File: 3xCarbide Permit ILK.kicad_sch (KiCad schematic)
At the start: 48 parts, among them J1 UT00104PH, J2 UT00104PH, J3 UT00104PH, J4 UT00104PH, J5 UT00104PH, J6 UT00104PH, SW1 2PB11, SW2 2PB11, SW3 2PB11, SW4 2PB11, SW5 2PB11, SW6 2PB11

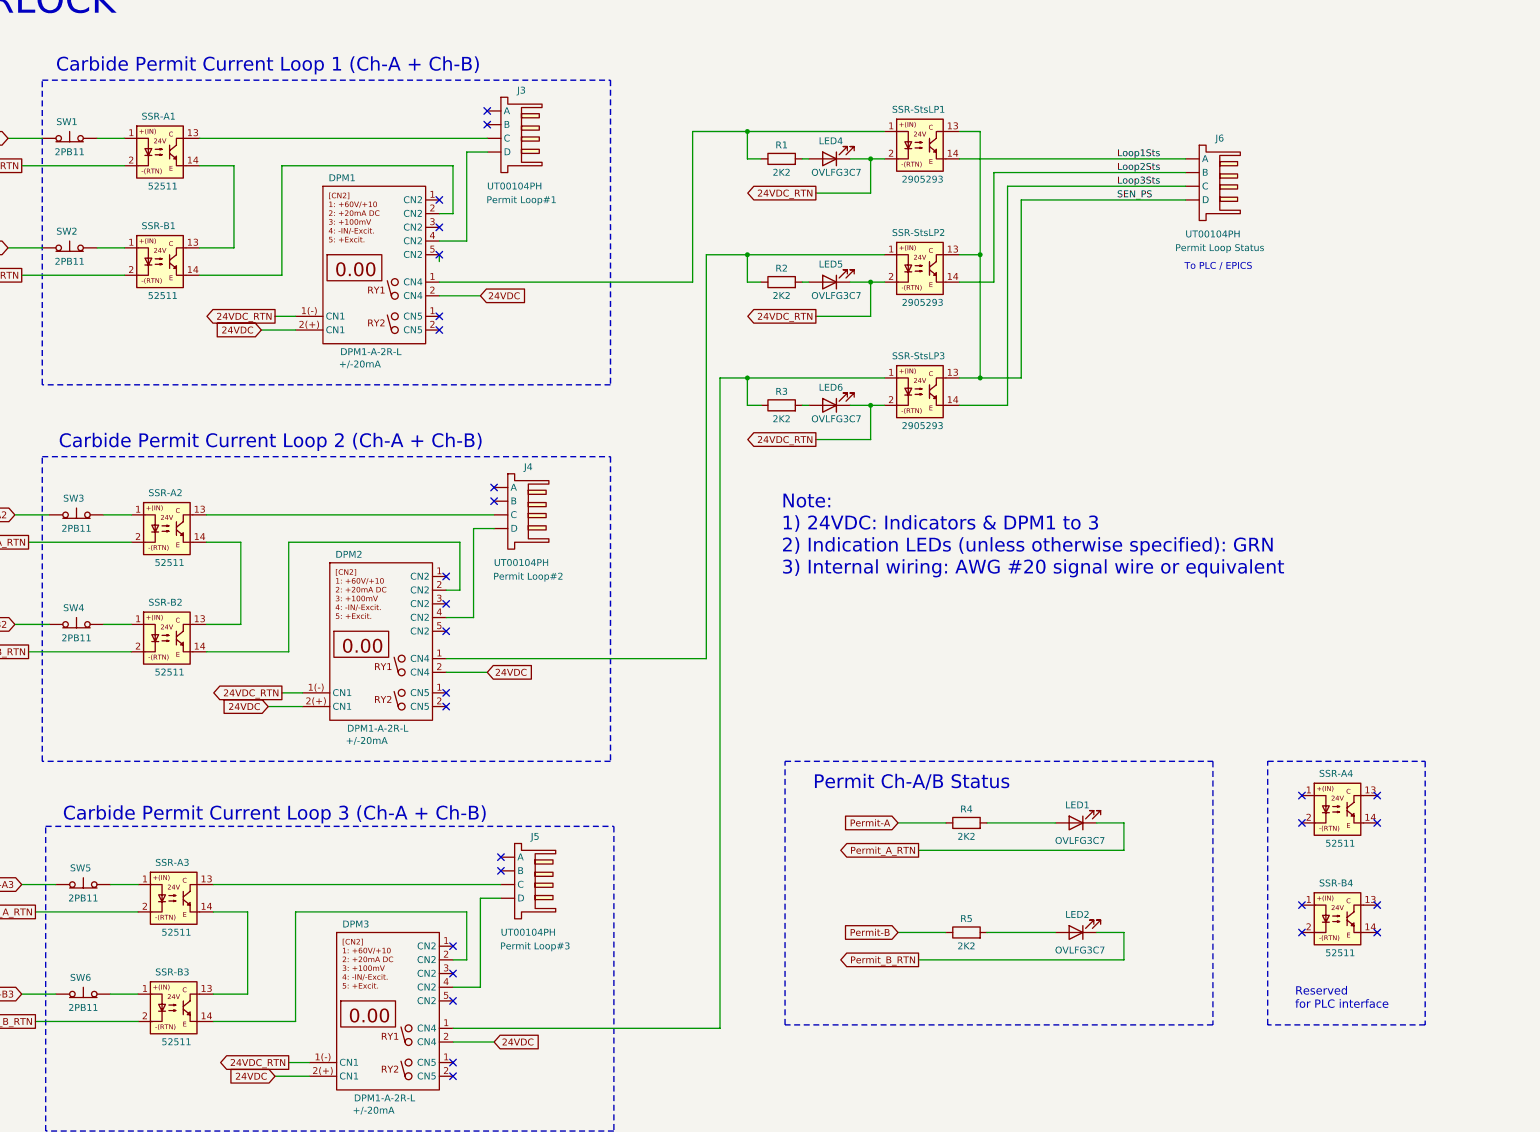
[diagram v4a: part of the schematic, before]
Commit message: updated SSR Pin and cleanup
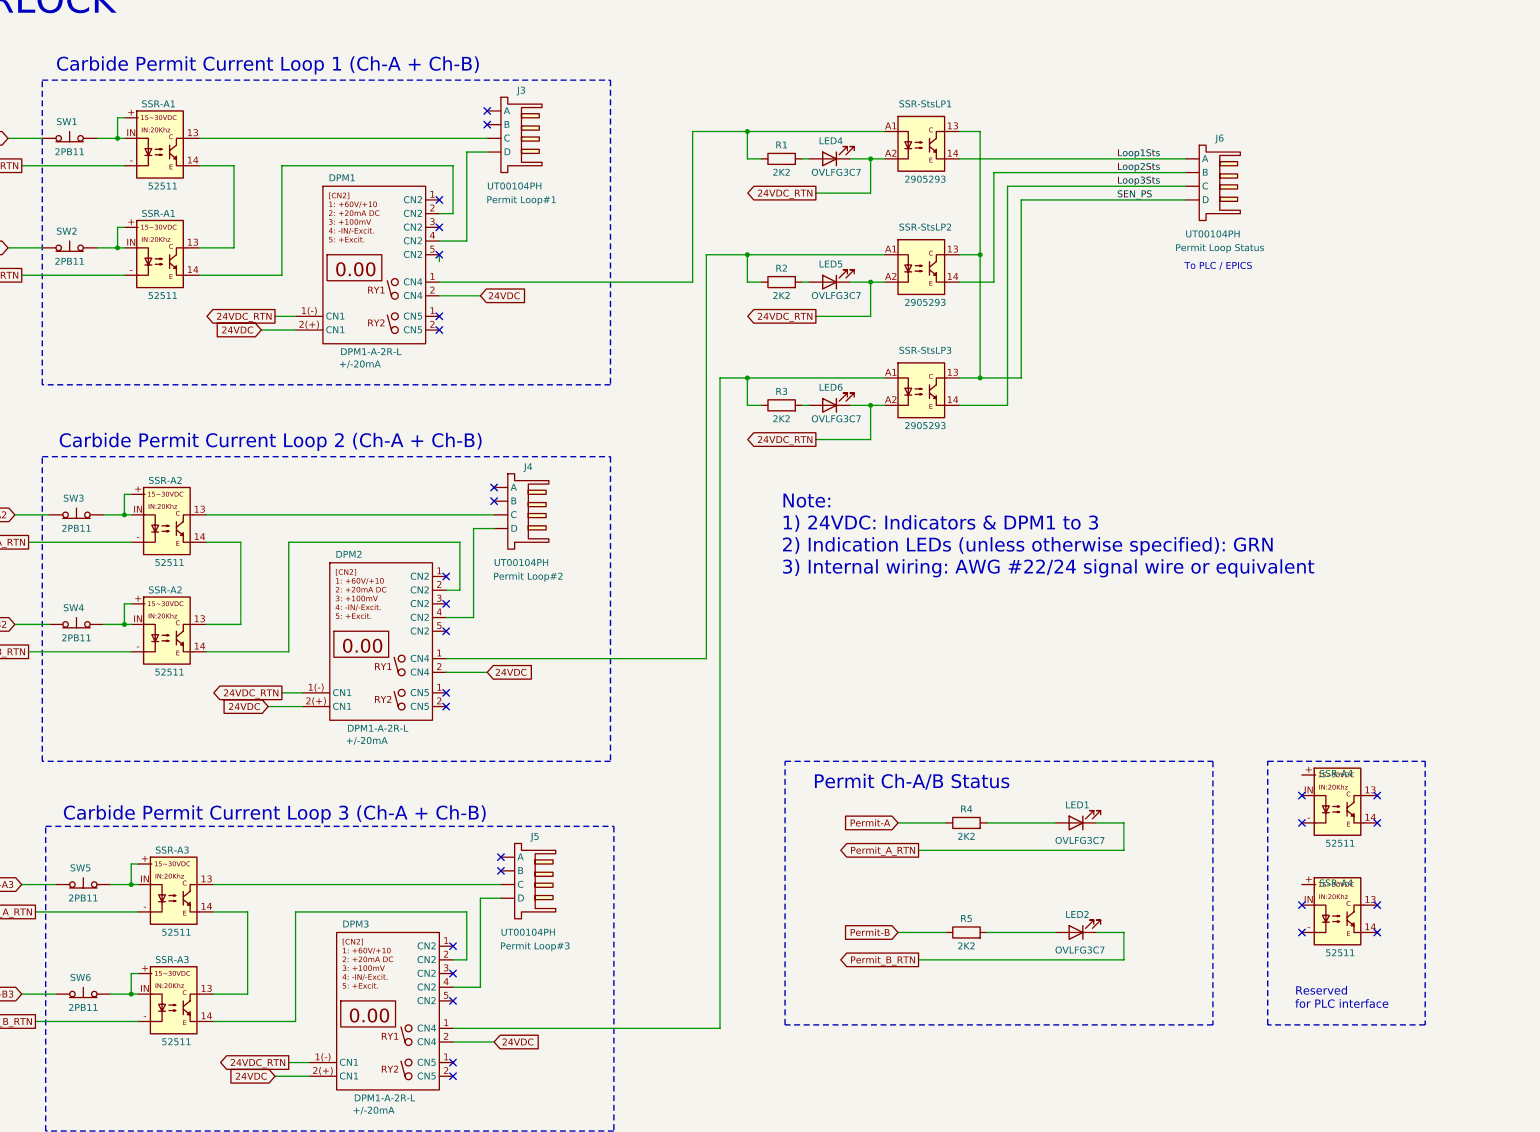
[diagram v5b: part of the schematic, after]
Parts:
- removed SSR-StsLP1, SSR-StsLP2, SSR-StsLP3: 2905293, symbol JP_3xCarbide:SSR_MIRO_52511
- added SSR-StsLP1, SSR-StsLP2, SSR-StsLP3: 2905293, symbol JP_3xCarbide:SSR_Phx2905293
- renumbered SSR-B1 to SSR-A1, SSR-B2 to SSR-A2, SSR-B3 to SSR-A3, SSR-B4 to SSR-A4
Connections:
- net 24VDC_RTN: now also SSR-StsLP1.A2, SSR-StsLP2.A2, SSR-StsLP3.A2
- net Loop1Sts: now also SSR-StsLP1.14
- net Loop2Sts: now also SSR-StsLP2.14
- net Loop3Sts: now also SSR-StsLP3.14
- net Permit_A_RTN: now also SSR-A1.-, SSR-A2.-, SSR-A3.-; no longer SSR-A1.2, SSR-A2.2, SSR-A3.2
- net Permit_B_RTN: now also SSR-A1.-, SSR-A2.-, SSR-A3.-; no longer SSR-A1.2, SSR-A2.2, SSR-A3.2
- net SEN_PS: now also SSR-StsLP1.13, SSR-StsLP2.13, SSR-StsLP3.13
- net at J2. (D): no longer TB-B1. (D)
- net at SW4.2 (B): now also SSR-A2.+, SSR-A2.IN; no longer SSR-A2.1
- net at DPM1.1 (CN5): now also R1.1, SSR-StsLP1.A1
- net at J1. (D): now also TB-A3. (D)
- net at DPM2.1 (CN5), R2.1: now also SSR-StsLP2.A1
- net at SW3.2 (B): now also SSR-A2.+, SSR-A2.IN; no longer SSR-A2.1
- net at SW2.2 (B): now also SSR-A1.+, SSR-A1.IN; no longer SSR-A1.1
- net at SW1.2 (B): now also SSR-A1.+, SSR-A1.IN; no longer SSR-A1.1
- net at DPM3.1 (CN5): now also R3.1, SSR-StsLP3.A1
- net at J4. (D): now also DPM2.4 (CN2)
- net at J5. (D): now also SSR-A3.13
- net at SW6.2 (B): now also SSR-A3.+, SSR-A3.IN; no longer SSR-A3.1
- net at SW5.2 (B): now also SSR-A3.+, SSR-A3.IN; no longer SSR-A3.1
- new net: J2. (D), TB-B1. (D)
- new net: J1. (D), TB-A1. (D)
- new net: J2. (D), TB-B3. (D)
- now unconnected: J2. (D)
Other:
- note added: "Note: 1) 24VDC: Indicators & DPM1 to 3 2) Indication LEDs (unless otherwise specified): GRN 3) Internal wiring: AWG #22/24 signal wire or equivalent"
- note removed: "Note: 1) 24VDC: Indicators & DPM1 to 3 2) Indication LEDs (unless otherwise specified): GRN 3) Internal wiring: AWG #20 signal wire or equivalent"

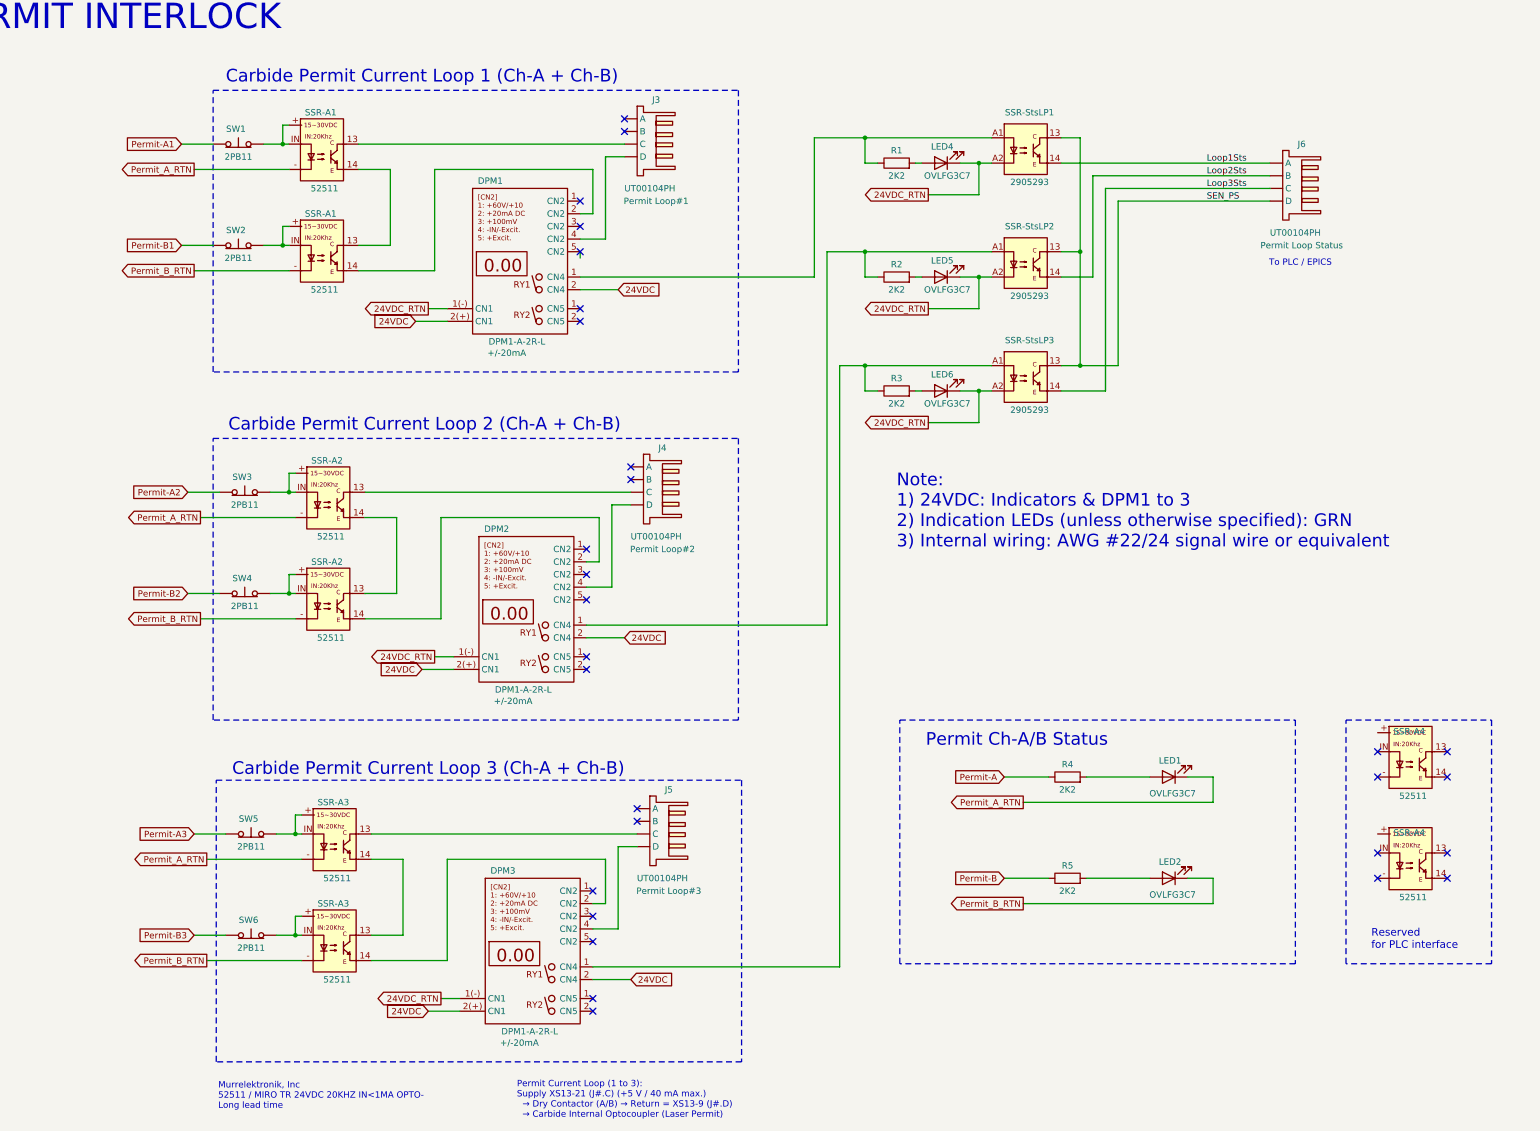
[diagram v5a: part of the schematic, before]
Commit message: added diode on MURR SSR
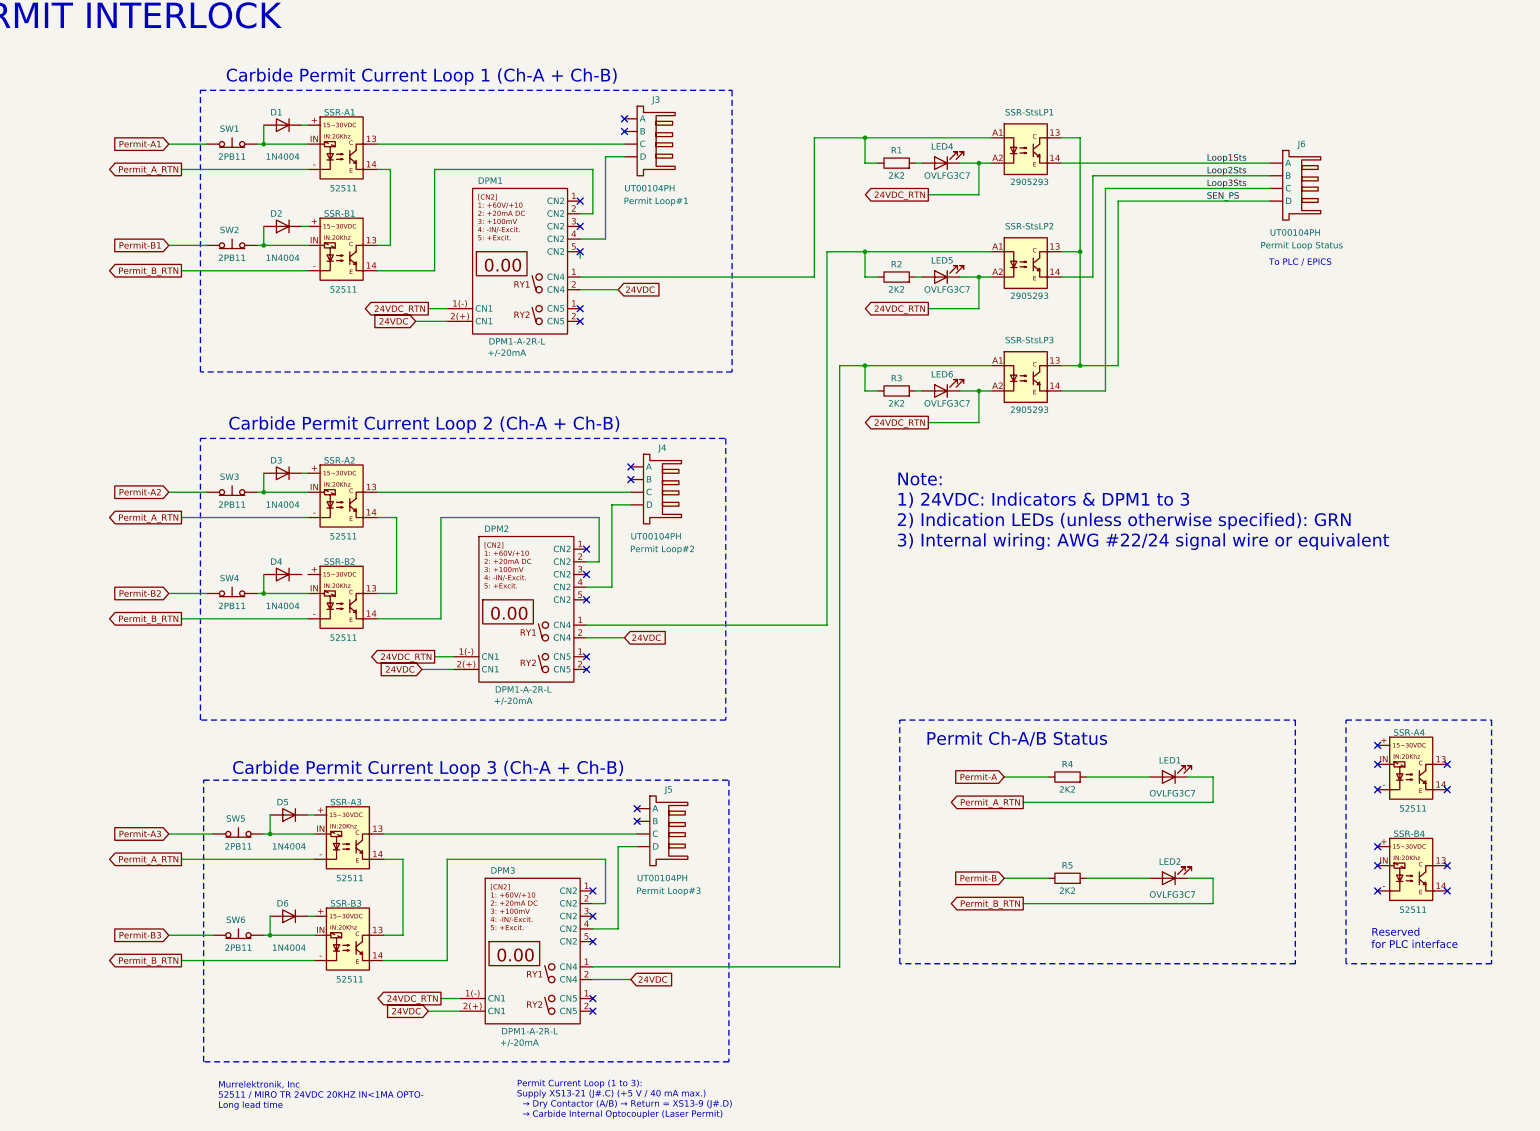
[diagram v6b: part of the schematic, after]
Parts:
- added D1, D2, D3, D4, D5, D6: 1N4004, Diode_THT:D_DO-41_SOD81_P10.16mm_Horizontal, symbol Diode:1N4004
- renumbered SSR-A1 to SSR-B1, SSR-A2 to SSR-B2, SSR-A3 to SSR-B3, SSR-A4 to SSR-B4
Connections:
- net at J2. (D): no longer TB-B1. (D)
- net at SSR-B2.IN, SW4.2 (B): now also D4.2 (A); no longer SSR-B2.+
- net at DPM1.1 (CN5): now also R1.1, SSR-StsLP1.A1
- net at J1. (D): now also TB-A3. (D)
- net at SSR-A2.IN, SW3.2 (B): now also D3.2 (A); no longer SSR-A2.+
- net at SSR-B1.IN, SW2.2 (B): now also D2.2 (A); no longer SSR-B1.+
- net at SSR-A1.IN, SW1.2 (B): now also D1.2 (A); no longer SSR-A1.+
- net at DPM3.1 (CN5): now also R3.1, SSR-StsLP3.A1
- net at J4. (D): now also DPM2.4 (CN2)
- net at J5. (D): now also SSR-A3.13
- net at SSR-B3.IN, SW6.2 (B): now also D6.2 (A); no longer SSR-B3.+
- net at SSR-A3.IN, SW5.2 (B): now also D5.2 (A); no longer SSR-A3.+
- new net: D3.1 (K), SSR-A2.+
- new net: J2. (D), TB-B1. (D)
- new net: D2.1 (K), SSR-B1.+
- new net: J1. (D), TB-A1. (D)
- new net: D1.1 (K), SSR-A1.+
- new net: J2. (D), TB-B3. (D)
- new net: D6.1 (K), SSR-B3.+
- new net: D5.1 (K), SSR-A3.+
- now unconnected: J2. (D)
- no-connect marks 44 -> 46
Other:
- moved on the sheet: SW1, SW2, SW3, SW4, SW5, SW6
